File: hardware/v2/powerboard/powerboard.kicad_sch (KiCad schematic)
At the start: 36 parts, among them J1 LEG1_PWR, J10 UBEC3, J11 SBEC, J12 LOGIC_5V_OUT, J13 MONITOR, J2 LEG2_PWR, J3 LEG3_PWR, J4 LEG4_PWR, J5 LEG5_PWR, J6 LEG6_PWR, J7 BATTERY, J8 UBEC1, J9 UBEC2, Q1 FQP47P06, Q2 FQP47P06, Q3 MMBT3904, SW1 MASTER_SW

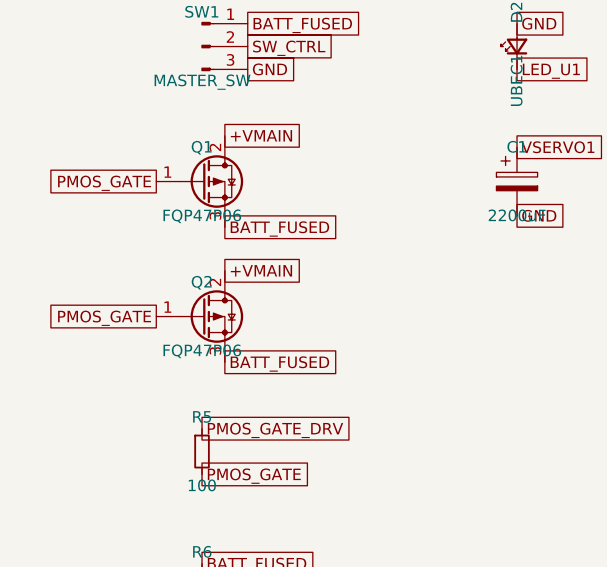
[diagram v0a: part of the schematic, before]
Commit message: hardware: fix legboard current-sense channel mapping, swap powerboard PMOS to IRF9540NPBF
Legboard: correct the INA4181 stub labels so U3 pins 2-4/13-15 map to
TOTAL/TIBIA current sensing per the corrected net table, instead of the
swapped TOTAL<->TIBIA assignment.

Powerboard: replace Q1/Q2 reverse-polarity PMOS (FQP47P06 -> IRF9540NPBF).
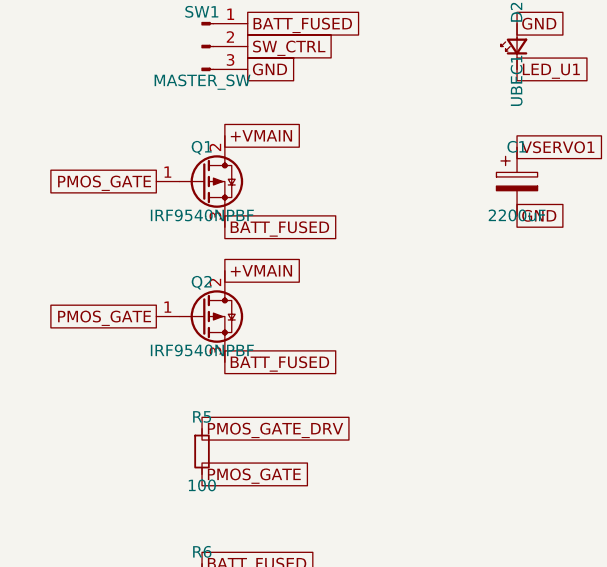
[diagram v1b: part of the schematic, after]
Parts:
- Q1, Q2: value FQP47P06 -> IRF9540NPBF
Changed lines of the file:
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@@
 			)
 		)
-		(property "Value" "FQP47P06"
+		(property "Value" "IRF9540NPBF"
 			(at 35 83.81 0)
 			(effects
@@
 			)
 		)
-		(property "Value" "FQP47P06"
+		(property "Value" "IRF9540NPBF"
 			(at 35 98.81 0)
 			(effects
